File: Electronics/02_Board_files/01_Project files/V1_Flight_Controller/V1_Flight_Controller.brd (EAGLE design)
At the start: 46.2 x 46.2 mm, 74 parts

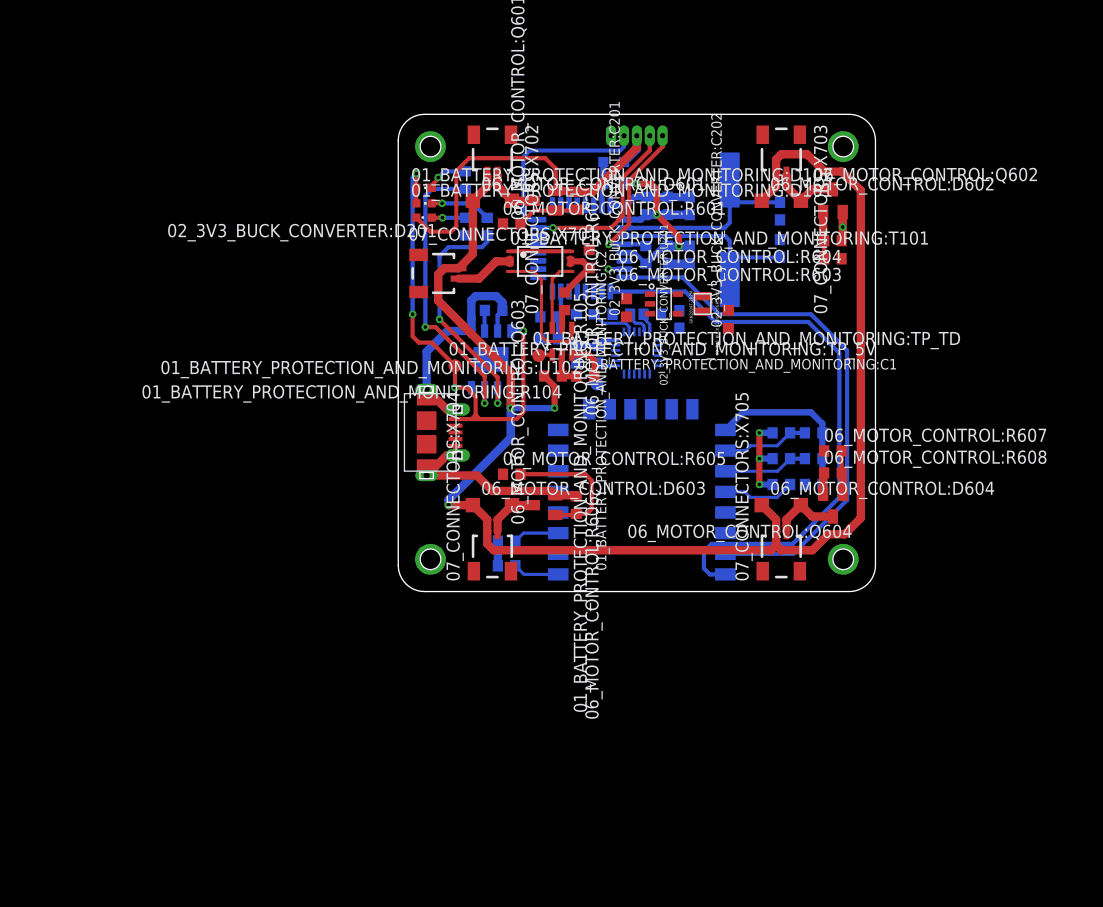
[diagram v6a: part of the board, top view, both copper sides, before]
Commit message: 1. Removed unnecessary pads in usb port 2. Completed placement and routing of first prototype
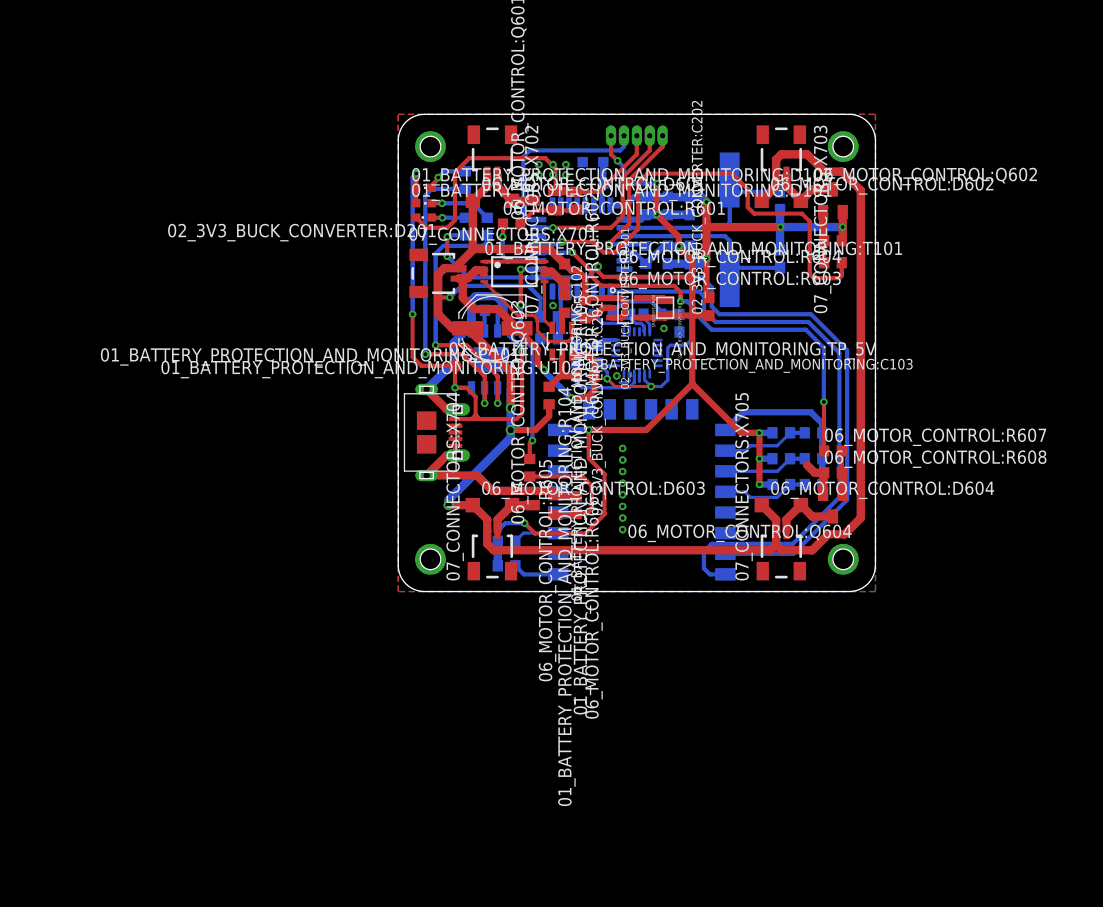
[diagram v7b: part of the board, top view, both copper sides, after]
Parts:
- removed 01_BATTERY_PROTECTION_AND_MONITORING:C2: 10uF, adafruit:C0603K
- removed 01_BATTERY_PROTECTION_AND_MONITORING:TP_TD, 05_SENSOR:TP_IMU_3V3: TPB1,27, testpad:B1,27
- added 01_BATTERY_PROTECTION_AND_MONITORING:C101: 220uF, adafruit:PANASONIC_D
- added 01_BATTERY_PROTECTION_AND_MONITORING:C102: 10uF, adafruit:C0603K
- moved 02_3V3_BUCK_CONVERTER:C201 4.00 mm to (18.1, 27.4), turned to 270 degrees
- moved 02_3V3_BUCK_CONVERTER:U201 3.77 mm to (22.0, 27.5)
- moved 02_3V3_BUCK_CONVERTER:L201 3.64 mm to (25.9, 27.5)
- moved 01_BATTERY_PROTECTION_AND_MONITORING:T101 2.69 mm to (11.2, 31.0)
- moved 02_3V3_BUCK_CONVERTER:C202 2.25 mm to (30.1, 27.6)
- moved 03_MICROCONTROLLER:L303 2.00 mm to (18.9, 41.6), turned to 0 degrees
- moved 01_BATTERY_PROTECTION_AND_MONITORING:R104 1.91 mm to (14.6, 19.0), turned to 270 degrees
- moved 06_MOTOR_CONTROL:R605 1.86 mm to (12.8, 12.0), turned to 270 degrees
- moved 03_MICROCONTROLLER:C306 1.00 mm to (37.0, 37.9)
- moved 03_MICROCONTROLLER:C307 1.00 mm to (37.0, 32.2)
- moved 05_SENSOR:C501 0.38 mm to (27.2, 26.0)
- moved 06_MOTOR_CONTROL:R603 0.38 mm to (42.1, 31.9)
- moved 01_BATTERY_PROTECTION_AND_MONITORING:R105 0.25 mm to (16.1, 27.9)
- renumbered 01_BATTERY_PROTECTION_AND_MONITORING:C1 to 01_BATTERY_PROTECTION_AND_MONITORING:C103
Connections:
- removed net 01_BATTERY_PROTECTION_AND_MONITORING:TD: 01_BATTERY_PROTECTION_AND_MONITORING:TP_TD.TP, 01_BATTERY_PROTECTION_AND_MONITORING:U102.4
- removed net ESP8266_RST: 03_MICROCONTROLLER:U301.7, 04_WIFI:R401.2, 04_WIFI:U401.1
- new net 04_WIFI:RST_ESP8266: 04_WIFI:R401.2, 04_WIFI:U401.1
- net +3V3: no longer 05_SENSOR:TP_IMU_3V3.TP
- net BATTERY_+VE: now also 01_BATTERY_PROTECTION_AND_MONITORING:C101.+, 01_BATTERY_PROTECTION_AND_MONITORING:C102.1; no longer 01_BATTERY_PROTECTION_AND_MONITORING:C2.1
- net BATTERY_-VE: now also 01_BATTERY_PROTECTION_AND_MONITORING:C101.-
- net GND: now also 01_BATTERY_PROTECTION_AND_MONITORING:C102.2; no longer 01_BATTERY_PROTECTION_AND_MONITORING:C2.2
- net M1_PWM: now also 03_MICROCONTROLLER:U301.19; no longer 03_MICROCONTROLLER:U301.18
- net M2_PWM: now also 03_MICROCONTROLLER:U301.21; no longer 03_MICROCONTROLLER:U301.19
- net M3_PWM: now also 03_MICROCONTROLLER:U301.18; no longer 03_MICROCONTROLLER:U301.20
- net M4_PWM: now also 03_MICROCONTROLLER:U301.20; no longer 03_MICROCONTROLLER:U301.21
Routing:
- net +3V3: track 36.9 -> 166.0 mm, vias 6 -> 14
- net M2_PWM: track 0.00 -> 45.3 mm, vias 0 -> 1
- net M4_PWM: track 0.00 -> 42.5 mm, vias 0 -> 3
- net BATTERY_+VE: track 145.4 -> 177.7 mm, vias 3 -> 4
- net GND: track 120.5 -> 151.8 mm, vias 1 -> 21
- net M3_PWM: track 0.00 -> 20.6 mm, vias 0 -> 3
- net BATTERY_-VE: track 10.2 -> 28.6 mm, vias 0 -> 2
- net 05_SENSOR:REGOUT: track 0.00 -> 8.75 mm
- net M1_PWM: track 0.00 -> 6.77 mm, vias 0 -> 1
- net ESP8266_RST: track 6.06 -> 0.00 mm, vias 1 -> 0
- net 04_WIFI:RST_ESP8266: track 0.00 -> 4.50 mm
- net 02_3V3_BUCK_CONVERTER:SW: track 0.00 -> 2.61 mm
- net 01_BATTERY_PROTECTION_AND_MONITORING:STDBY: track 23.9 -> 26.3 mm
- net 01_BATTERY_PROTECTION_AND_MONITORING:OC: track 6.80 -> 4.79 mm
- net 01_BATTERY_PROTECTION_AND_MONITORING:VCC: track 3.49 -> 5.22 mm
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- added copper zone on layer 1, net GND
- added copper zone on layer 16, net GND
